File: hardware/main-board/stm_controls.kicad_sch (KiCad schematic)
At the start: 56 parts, among them J10 Conn_02x05_Odd_Even, J11 Conn_01x02_Pin, J9 USB_C_Receptacle_USB2.0_14P, SW3 SW_SPST, SW4 SW_SPST, U1 MT8816AF1, U11 MT8816AF1, U12 MT8816AF1, U14 AD5263BRUZ200, U15 AD5263BRUZ200, U17 MT8816AF1, U18 MT8816AF1, U20 AD5263BRUZ200, U21 AD5263BRUZ200, U23 MT8816AF1, U24 MT8816AF1, U26 AD5263BRUZ200, U27 AD5263BRUZ200, U29 MT8816AF1, U30 MT8816AF1, U34 74HC164, U35 FT232RL, U36 74HC164, U37 STM32F091RCTx, U38 74HC164, U8 AD5263BRUZ200, U9 AD5263BRUZ200

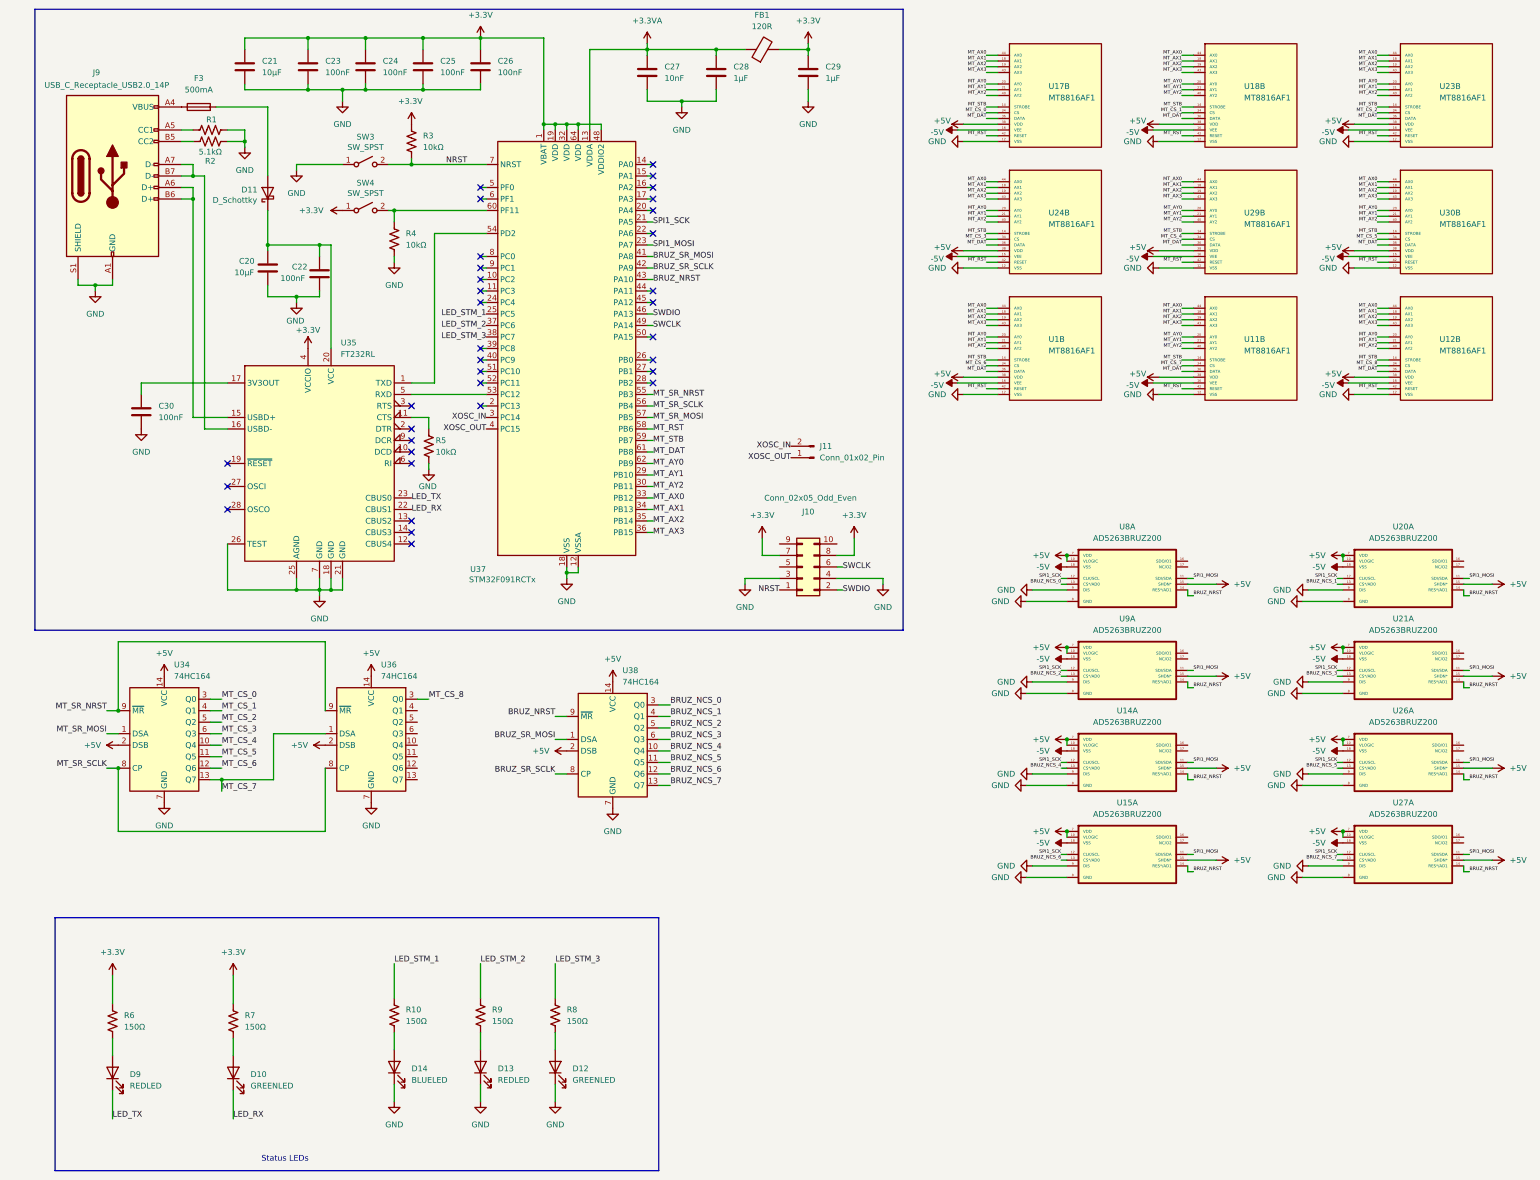
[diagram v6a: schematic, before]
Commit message: designed Power PCB section layout
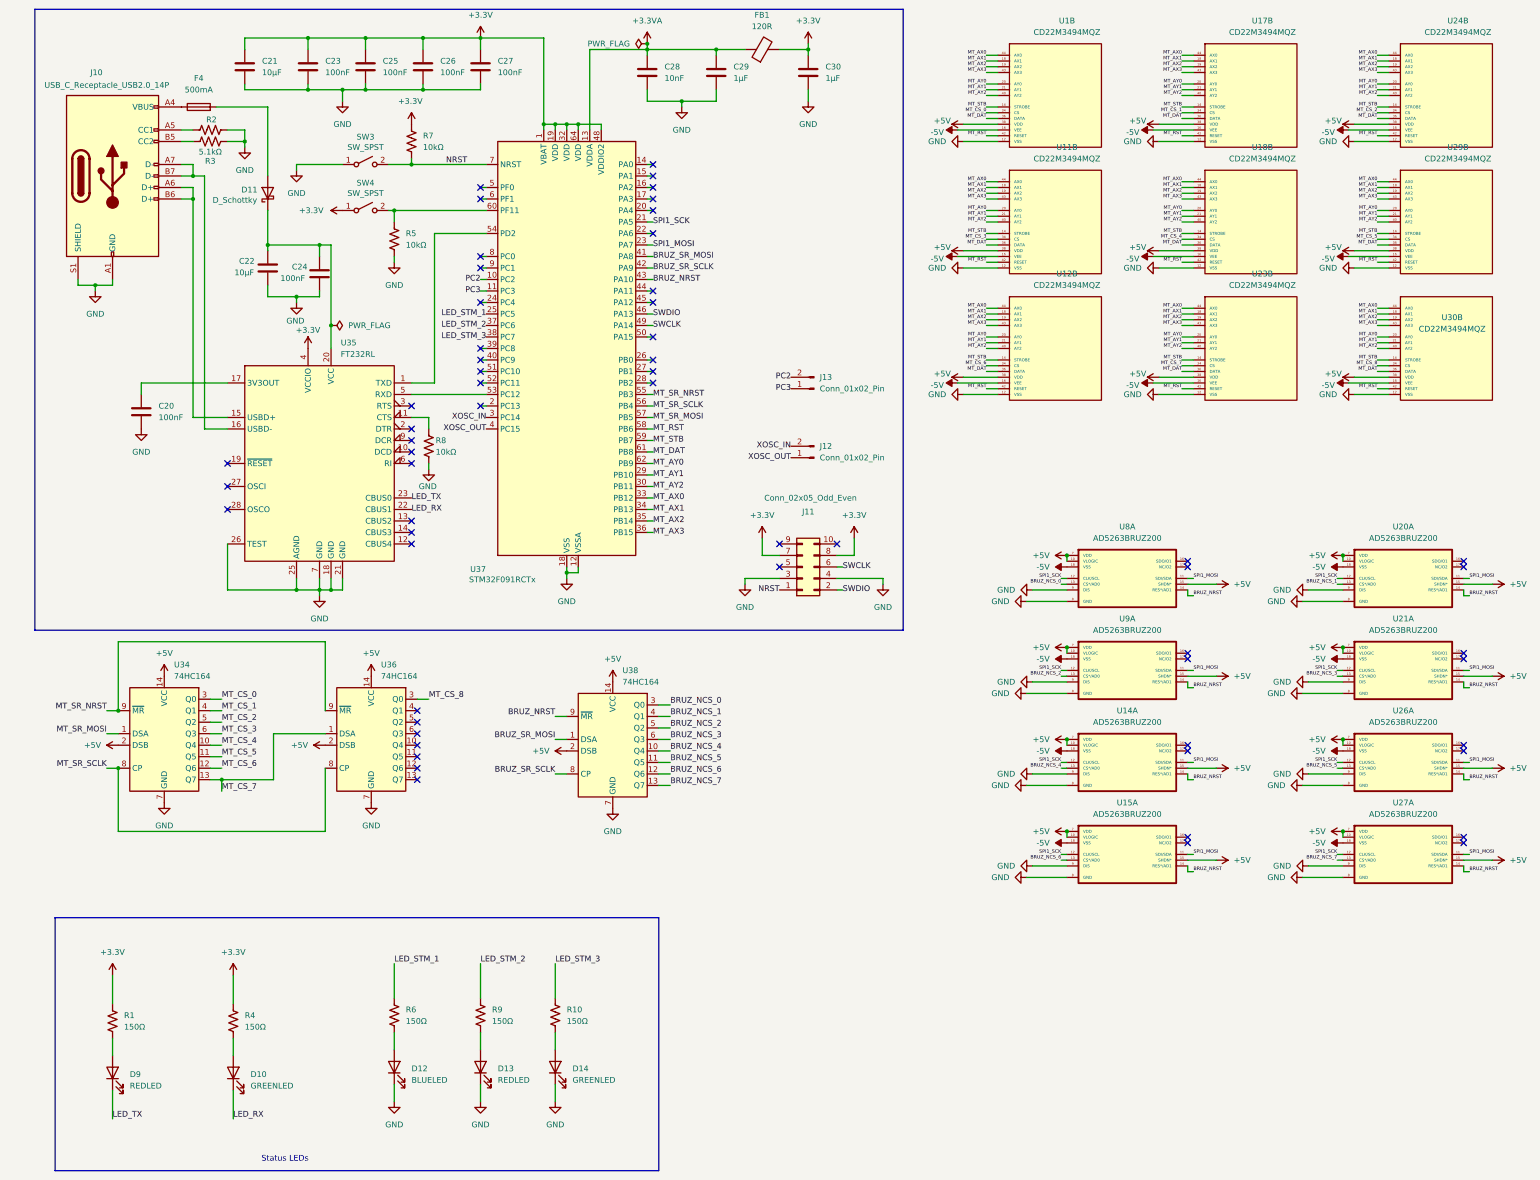
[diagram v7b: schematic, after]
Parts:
- removed U1, U11, U12, U17, U18, U23, U24, U29, U30: MT8816AF1, SeniorDesignFP:QFP80P1200X1200X120-44N, symbol SeniorDesign:MT8816AF1
- added J13: Conn_01x02_Pin, Connector_PinHeader_1.00mm:PinHeader_1x02_P1.00mm_Horizontal, symbol Connector:Conn_01x02_Pin
- added U1, U11, U12, U17, U18, U23, U24, U29, U30: CD22M3494MQZ, SeniorDesignFP:PLCC44_16P66X16P66_INR-M, symbol SeniorDesign:CD22M3494MQZ
- renumbered C30 to C20, C20 to C22, C22 to C24, C24 to C25, C25 to C26, C26 to C27, C27 to C28, C28 to C29, C29 to C30, D14 to D12, D12 to D14, F3 to F4, J9 to J10, J10 to J11, J11 to J12, R6 to R1, R8 to R10, R1 to R2, R2 to R3, R7 to R4, R4 to R5, R10 to R6, R3 to R7, R5 to R8
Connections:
- net +5V: now also U1.38 (VDD), U11.38 (VDD), U12.38 (VDD), U17.38 (VDD), U18.38 (VDD), U23.38 (VDD), U24.38 (VDD), U29.38 (VDD), U30.38 (VDD)
- net -5V: now also U1.16 (VEE), U11.16 (VEE), U12.16 (VEE), U17.16 (VEE), U18.16 (VEE), U23.16 (VEE), U24.16 (VEE), U29.16 (VEE), U30.16 (VEE)
- net GND: now also U1.12 (VSS), U11.12 (VSS), U12.12 (VSS), U17.12 (VSS), U18.12 (VSS), U23.12 (VSS), U24.12 (VSS), U29.12 (VSS), U30.12 (VSS)
- net MT_AX0: now also U1.44 (AX0), U11.44 (AX0), U12.44 (AX0), U17.44 (AX0), U18.44 (AX0), U23.44 (AX0), U24.44 (AX0), U29.44 (AX0), U30.44 (AX0)
- net MT_AX1: now also U1.18 (AX1), U11.18 (AX1), U12.18 (AX1), U17.18 (AX1), U18.18 (AX1), U23.18 (AX1), U24.18 (AX1), U29.18 (AX1), U30.18 (AX1)
- net MT_AX2: now also U1.19 (AX2), U11.19 (AX2), U12.19 (AX2), U17.19 (AX2), U18.19 (AX2), U23.19 (AX2), U24.19 (AX2), U29.19 (AX2), U30.19 (AX2)
- net MT_AX3: now also U1.43 (AX3), U11.43 (AX3), U12.43 (AX3), U17.43 (AX3), U18.43 (AX3), U23.43 (AX3), U24.43 (AX3), U29.43 (AX3), U30.43 (AX3)
- net MT_AY0: now also U1.20 (AY0), U11.20 (AY0), U12.20 (AY0), U17.20 (AY0), U18.20 (AY0), U23.20 (AY0), U24.20 (AY0), U29.20 (AY0), U30.20 (AY0)
- net MT_AY1: now also U1.21 (AY1), U11.21 (AY1), U12.21 (AY1), U17.21 (AY1), U18.21 (AY1), U23.21 (AY1), U24.21 (AY1), U29.21 (AY1), U30.21 (AY1)
- net MT_AY2: now also U1.40 (AY2), U11.40 (AY2), U12.40 (AY2), U17.40 (AY2), U18.40 (AY2), U23.40 (AY2), U24.40 (AY2), U29.40 (AY2), U30.40 (AY2)
- net MT_CS_0: now also U1.34 (CS)
- net MT_CS_1: now also U17.34 (CS)
- net MT_CS_2: now also U24.34 (CS)
- net MT_CS_3: now also U11.34 (CS)
- net MT_CS_4: now also U18.34 (CS)
- net MT_CS_5: now also U29.34 (CS)
- net MT_CS_6: now also U12.34 (CS)
- net MT_CS_7: now also U23.34 (CS)
- net MT_CS_8: now also U30.34 (CS)
- net MT_DAT: now also U1.36 (DATA), U11.36 (DATA), U12.36 (DATA), U17.36 (DATA), U18.36 (DATA), U23.36 (DATA), U24.36 (DATA), U29.36 (DATA), U30.36 (DATA)
- net MT_RST: now also U1.42 (RESET), U11.42 (RESET), U12.42 (RESET), U17.42 (RESET), U18.42 (RESET), U23.42 (RESET), U24.42 (RESET), U29.42 (RESET), U30.42 (RESET)
- net MT_STB: now also U1.14 (STROBE), U11.14 (STROBE), U12.14 (STROBE), U17.14 (STROBE), U18.14 (STROBE), U23.14 (STROBE), U24.14 (STROBE), U29.14 (STROBE), U30.14 (STROBE)
- net PC2: now reaches U37.10 (PC2)
- net PC2: now also J13.2 (Pin_2)
- net PC3: now reaches U37.11 (PC3)
- net PC3: now also J13.1 (Pin_1)
- no-connect marks 35 -> 59
